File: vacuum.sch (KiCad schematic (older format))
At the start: 67 parts, among them J1 к БП, J10 геркон шибера 1, J11 запасной, J12 запасной, J13 к БП, J2 нагрузка, J3 нагрузка, J4 геркон клапана 0, J5 нагрузка, J6 нагрузка, J7 к БП, J8 геркон клапана 1, J9 геркон шибера 0, Q1 IRF740, Q2 IRF740, Q3 IRF740, Q4 IRF740, SW1 Кнопка, SW2 Кнопка, SW3 Кнопка, SW4 Выключить автоматику, SW5 Кнопка, U1 PC817, U10 PC817, U2 PC817, U3 PC817, U4 PC817, U5 PC817, U6 PC817, U7 PC817, U8 PC817, U9 PC817

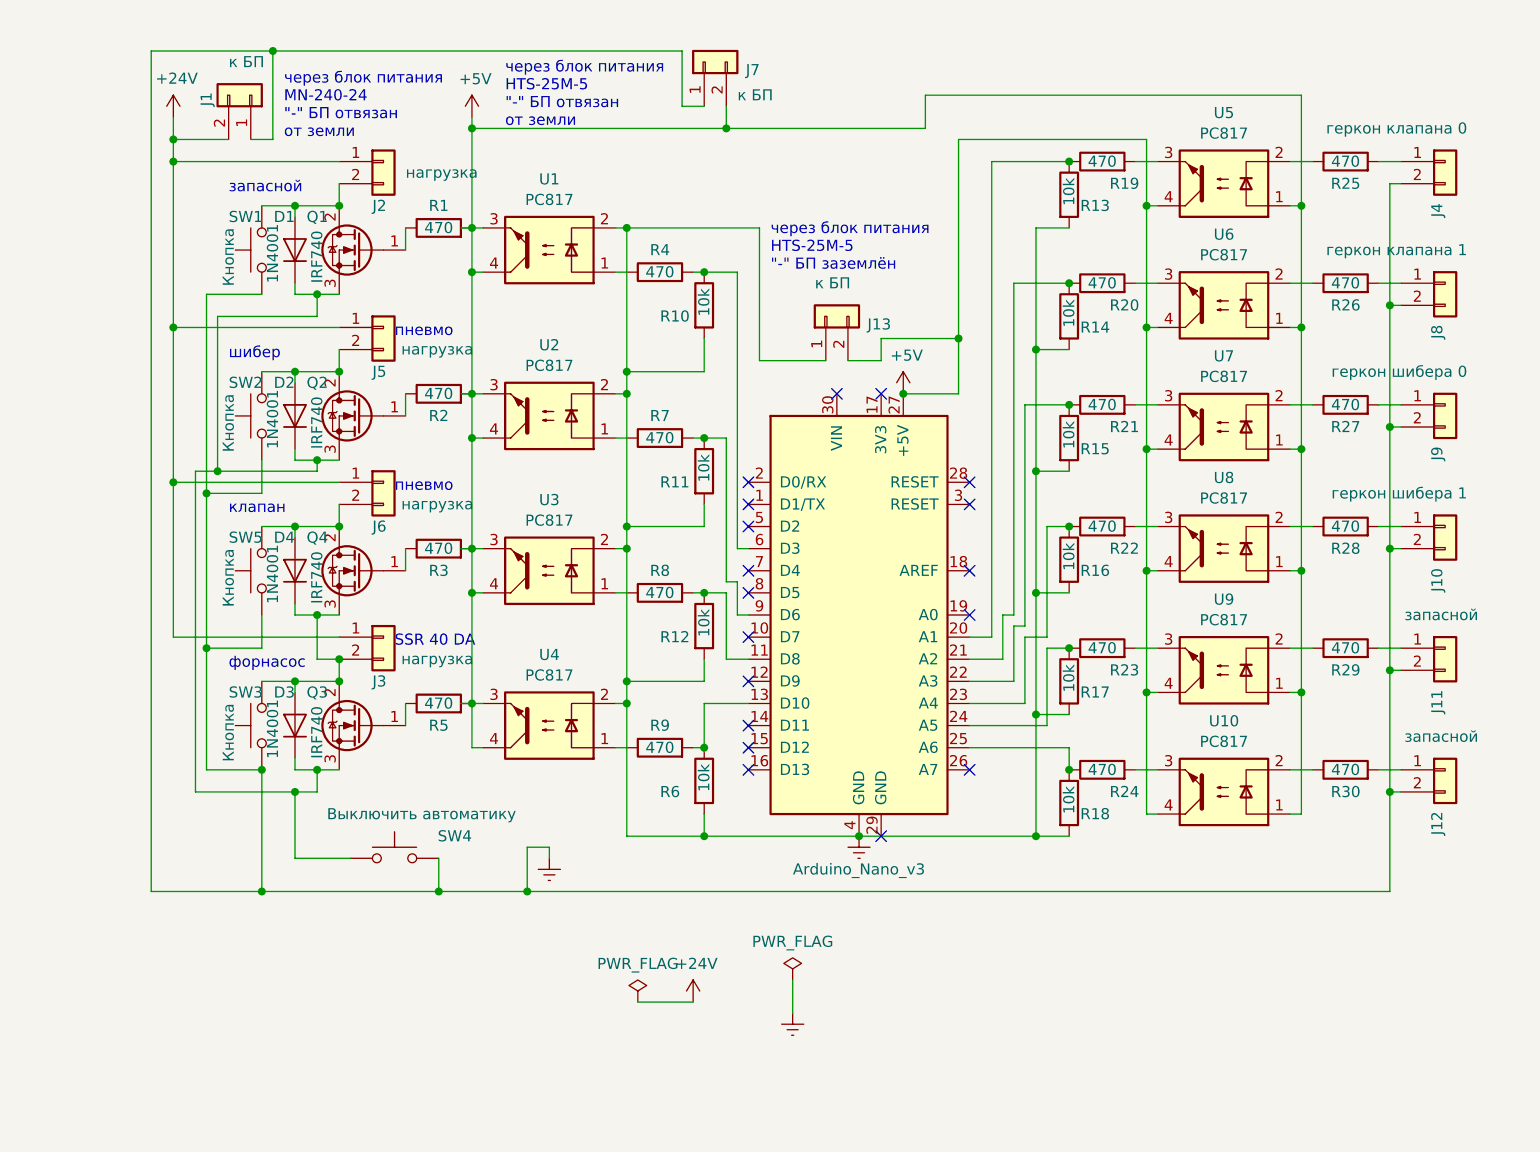
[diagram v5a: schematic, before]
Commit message: some important bags in *.sch removed, PCB partially created
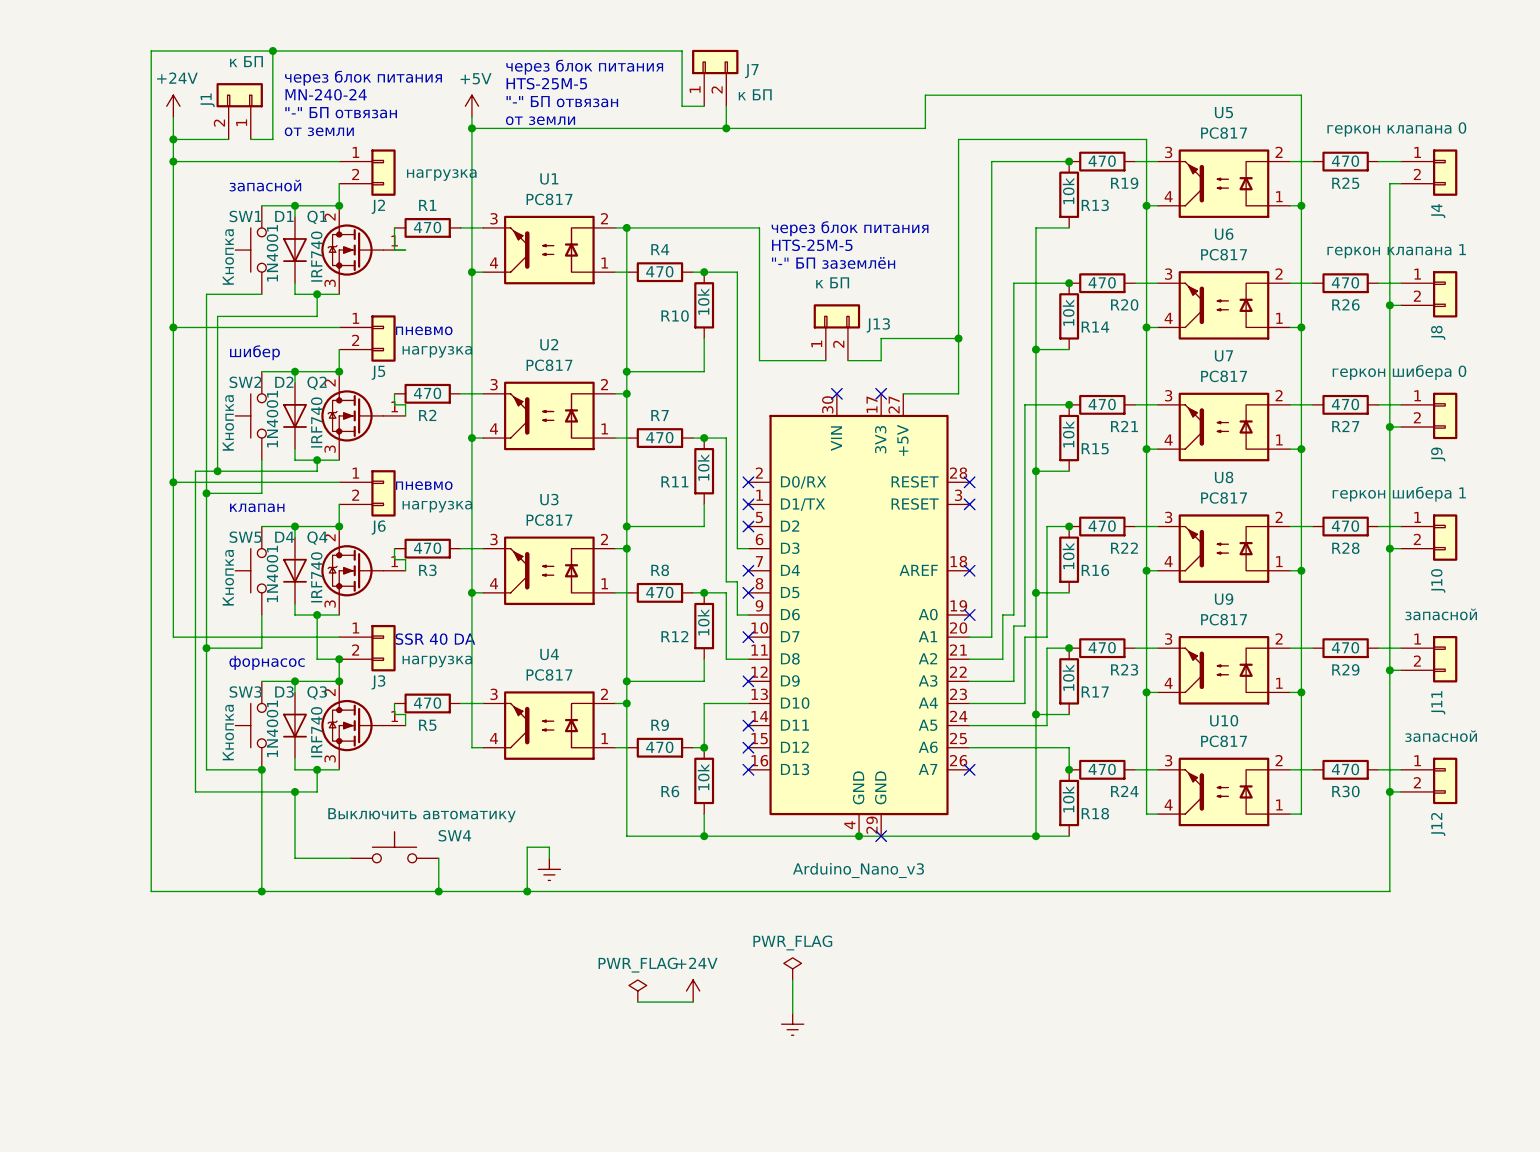
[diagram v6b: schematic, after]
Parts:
- SW1, SW2, SW3, SW5: footprint Button_Switch_THT:SW_PUSH_6mm_H5mm -> Connector_PinHeader_2.54mm:PinHeader_1x02_P2.54mm_Vertical
- SW4: footprint Button_Switch_THT:SW_PUSH_6mm -> TerminalBlock_Altech:Altech_AK300_1x02_P5.00mm_45-Degree
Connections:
- net +5V: no longer A1.27 (+5V), J13.2 (Pin_2), R1.2, R2.2, R3.2, R5.2, U1.3, U10.4, U2.3, U3.3, U4.3, U5.4, U6.4, U7.4, U8.4, U9.4
- net Earth: no longer A1.4 (GND), J13.1 (Pin_1), R10.2, R11.2, R12.2, R13.2, R14.2, R15.2, R16.2, R17.2, R18.2, R6.2, U1.2, U2.2, U3.2, U4.2
- new net: A1.27 (+5V), J13.2 (Pin_2), U10.4, U5.4, U6.4, U7.4, U8.4, U9.4
- new net: A1.4 (GND), J13.1 (Pin_1), R10.2, R11.2, R12.2, R13.2, R14.2, R15.2, R16.2, R17.2, R18.2, R6.2, U1.2, U2.2, U3.2, U4.2
- new net: R5.2, U4.3
- new net: R3.2, U3.3
- new net: R2.2, U2.3
- new net: R1.2, U1.3
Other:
- moved on the sheet: R1, R2, R3, R5

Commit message: vertical resistors aded
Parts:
- R1, R19, R2, R20, R21, R22, R23, R24, R25, R26, R27, R28, R29, R3, R30, R4, R7, R8, R9: footprint Resistor_THT:R_Axial_DIN0207_L6.3mm_D2.5mm_P7.62mm_Horizontal -> Resistor_THT:R_Axial_DIN0207_L6.3mm_D2.5mm_P5.08mm_Vertical
- R10, R11, R12, R13, R14, R15, R16, R17, R18, R6: footprint Resistor_THT:R_Axial_DIN0309_L9.0mm_D3.2mm_P12.70mm_Horizontal -> Resistor_THT:R_Axial_DIN0309_L9.0mm_D3.2mm_P5.08mm_Vertical
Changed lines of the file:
@@
 F 0 "R6" H 4050 5800 50  0000 L CNN
 F 1 "10k" V 4250 5800 50  0000 L CNN
-F 2 "Resistor_THT:R_Axial_DIN0309_L9.0mm_D3.2mm_P12.70mm_Horizontal" V 4180 5850 50  0001 C CNN
+F 2 "Resistor_THT:R_Axial_DIN0309_L9.0mm_D3.2mm_P5.08mm_Vertical" V 4180 5850 50  0001 C CNN
 F 3 "~" H 4250 5850 50  0001 C CNN
 	1    4250 5850
@@
 F 0 "R9" V 4150 5700 50  0000 C CNN
 F 1 "470" V 4050 5700 50  0000 C CNN
-F 2 "Resistor_THT:R_Axial_DIN0207_L6.3mm_D2.5mm_P7.62mm_Horizontal" V 3980 5700 50  0001 C CNN
+F 2 "Resistor_THT:R_Axial_DIN0207_L6.3mm_D2.5mm_P5.08mm_Vertical" V 3980 5700 50  0001 C CNN
 F 3 "~" H 4050 5700 50  0001 C CNN
 	1    4050 5700
@@
 F 0 "R12" H 4050 5100 50  0000 L CNN
 F 1 "10k" V 4250 5100 50  0000 L CNN
-F 2 "Resistor_THT:R_Axial_DIN0309_L9.0mm_D3.2mm_P12.70mm_Horizontal" V 4180 5150 50  0001 C CNN
+F 2 "Resistor_THT:R_Axial_DIN0309_L9.0mm_D3.2mm_P5.08mm_Vertical" V 4180 5150 50  0001 C CNN
 F 3 "~" H 4250 5150 50  0001 C CNN
 	1    4250 5150
@@
 F 0 "R8" V 4150 5000 50  0000 C CNN
 F 1 "470" V 4050 5000 50  0000 C CNN
-F 2 "Resistor_THT:R_Axial_DIN0207_L6.3mm_D2.5mm_P7.62mm_Horizontal" V 3980 5000 50  0001 C CNN
+F 2 "Resistor_THT:R_Axial_DIN0207_L6.3mm_D2.5mm_P5.08mm_Vertical" V 3980 5000 50  0001 C CNN
 F 3 "~" H 4050 5000 50  0001 C CNN
 	1    4050 5000
@@
 F 0 "R11" H 4050 4400 50  0000 L CNN
 F 1 "10k" V 4250 4400 50  0000 L CNN
-F 2 "Resistor_THT:R_Axial_DIN0309_L9.0mm_D3.2mm_P12.70mm_Horizontal" V 4180 4450 50  0001 C CNN
+F 2 "Resistor_THT:R_Axial_DIN0309_L9.0mm_D3.2mm_P5.08mm_Vertical" V 4180 4450 50  0001 C CNN
 F 3 "~" H 4250 4450 50  0001 C CNN
 	1    4250 4450
@@
 F 0 "R7" V 4150 4300 50  0000 C CNN
 F 1 "470" V 4050 4300 50  0000 C CNN
-F 2 "Resistor_THT:R_Axial_DIN0207_L6.3mm_D2.5mm_P7.62mm_Horizontal" V 3980 4300 50  0001 C CNN
+F 2 "Resistor_THT:R_Axial_DIN0207_L6.3mm_D2.5mm_P5.08mm_Vertical" V 3980 4300 50  0001 C CNN
 F 3 "~" H 4050 4300 50  0001 C CNN
 	1    4050 4300
@@
 F 0 "R1" V 3100 3350 50  0000 C CNN
 F 1 "470" V 3000 3350 50  0000 C CNN
-F 2 "Resistor_THT:R_Axial_DIN0207_L6.3mm_D2.5mm_P7.62mm_Horizontal" V 2930 3350 50  0001 C CNN
+F 2 "Resistor_THT:R_Axial_DIN0207_L6.3mm_D2.5mm_P5.08mm_Vertical" V 2930 3350 50  0001 C CNN
 F 3 "~" H 3000 3350 50  0001 C CNN
 	1    3000 3350
@@
 F 0 "R10" H 4050 3650 50  0000 L CNN
 F 1 "10k" V 4250 3650 50  0000 L CNN
-F 2 "Resistor_THT:R_Axial_DIN0309_L9.0mm_D3.2mm_P12.70mm_Horizontal" V 4180 3700 50  0001 C CNN
+F 2 "Resistor_THT:R_Axial_DIN0309_L9.0mm_D3.2mm_P5.08mm_Vertical" V 4180 3700 50  0001 C CNN
 F 3 "~" H 4250 3700 50  0001 C CNN
 	1    4250 3700
@@
 F 0 "R4" V 4150 3550 50  0000 C CNN
 F 1 "470" V 4050 3550 50  0000 C CNN
-F 2 "Resistor_THT:R_Axial_DIN0207_L6.3mm_D2.5mm_P7.62mm_Horizontal" V 3980 3550 50  0001 C CNN
+F 2 "Resistor_THT:R_Axial_DIN0207_L6.3mm_D2.5mm_P5.08mm_Vertical" V 3980 3550 50  0001 C CNN
 F 3 "~" H 4050 3550 50  0001 C CNN
 	1    4050 3550
@@
 F 0 "R24" V 5950 5700 50  0000 C CNN
 F 1 "470" V 6050 5800 50  0000 C CNN
-F 2 "Resistor_THT:R_Axial_DIN0207_L6.3mm_D2.5mm_P7.62mm_Horizontal" V 5980 5800 50  0001 C CNN
+F 2 "Resistor_THT:R_Axial_DIN0207_L6.3mm_D2.5mm_P5.08mm_Vertical" V 5980 5800 50  0001 C CNN
 F 3 "~" H 6050 5800 50  0001 C CNN
 	1    6050 5800
@@
 F 0 "R18" H 5950 5900 50  0000 L CNN
 F 1 "10k" V 5900 5900 50  0000 L CNN
-F 2 "Resistor_THT:R_Axial_DIN0309_L9.0mm_D3.2mm_P12.70mm_Horizontal" V 5830 5950 50  0001 C CNN
+F 2 "Resistor_THT:R_Axial_DIN0309_L9.0mm_D3.2mm_P5.08mm_Vertical" V 5830 5950 50  0001 C CNN
 F 3 "~" H 5900 5950 50  0001 C CNN
 	1    5900 5950
@@
 F 0 "R23" V 5950 5150 50  0000 C CNN
 F 1 "470" V 6050 5250 50  0000 C CNN
-F 2 "Resistor_THT:R_Axial_DIN0207_L6.3mm_D2.5mm_P7.62mm_Horizontal" V 5980 5250 50  0001 C CNN
+F 2 "Resistor_THT:R_Axial_DIN0207_L6.3mm_D2.5mm_P5.08mm_Vertical" V 5980 5250 50  0001 C CNN
 F 3 "~" H 6050 5250 50  0001 C CNN
 	1    6050 5250
@@
 F 0 "R17" H 5950 5350 50  0000 L CNN
 F 1 "10k" V 5900 5350 50  0000 L CNN
-F 2 "Resistor_THT:R_Axial_DIN0309_L9.0mm_D3.2mm_P12.70mm_Horizontal" V 5830 5400 50  0001 C CNN
+F 2 "Resistor_THT:R_Axial_DIN0309_L9.0mm_D3.2mm_P5.08mm_Vertical" V 5830 5400 50  0001 C CNN
 F 3 "~" H 5900 5400 50  0001 C CNN
 	1    5900 5400
@@
 F 0 "R22" V 5950 4600 50  0000 C CNN
 F 1 "470" V 6050 4700 50  0000 C CNN
-F 2 "Resistor_THT:R_Axial_DIN0207_L6.3mm_D2.5mm_P7.62mm_Horizontal" V 5980 4700 50  0001 C CNN
+F 2 "Resistor_THT:R_Axial_DIN0207_L6.3mm_D2.5mm_P5.08mm_Vertical" V 5980 4700 50  0001 C CNN
 F 3 "~" H 6050 4700 50  0001 C CNN
 	1    6050 4700
@@
 F 0 "R16" H 5950 4800 50  0000 L CNN
 F 1 "10k" V 5900 4800 50  0000 L CNN
-F 2 "Resistor_THT:R_Axial_DIN0309_L9.0mm_D3.2mm_P12.70mm_Horizontal" V 5830 4850 50  0001 C CNN
+F 2 "Resistor_THT:R_Axial_DIN0309_L9.0mm_D3.2mm_P5.08mm_Vertical" V 5830 4850 50  0001 C CNN
 F 3 "~" H 5900 4850 50  0001 C CNN
 	1    5900 4850
@@
 F 0 "R21" V 5950 4050 50  0000 C CNN
 F 1 "470" V 6050 4150 50  0000 C CNN
-F 2 "Resistor_THT:R_Axial_DIN0207_L6.3mm_D2.5mm_P7.62mm_Horizontal" V 5980 4150 50  0001 C CNN
+F 2 "Resistor_THT:R_Axial_DIN0207_L6.3mm_D2.5mm_P5.08mm_Vertical" V 5980 4150 50  0001 C CNN
 F 3 "~" H 6050 4150 50  0001 C CNN
 	1    6050 4150
@@
 F 0 "R15" H 5950 4250 50  0000 L CNN
 F 1 "10k" V 5900 4250 50  0000 L CNN
-F 2 "Resistor_THT:R_Axial_DIN0309_L9.0mm_D3.2mm_P12.70mm_Horizontal" V 5830 4300 50  0001 C CNN
+F 2 "Resistor_THT:R_Axial_DIN0309_L9.0mm_D3.2mm_P5.08mm_Vertical" V 5830 4300 50  0001 C CNN
 F 3 "~" H 5900 4300 50  0001 C CNN
 	1    5900 4300
@@
 F 0 "R20" V 5950 3500 50  0000 C CNN
 F 1 "470" V 6050 3600 50  0000 C CNN
-F 2 "Resistor_THT:R_Axial_DIN0207_L6.3mm_D2.5mm_P7.62mm_Horizontal" V 5980 3600 50  0001 C CNN
+F 2 "Resistor_THT:R_Axial_DIN0207_L6.3mm_D2.5mm_P5.08mm_Vertical" V 5980 3600 50  0001 C CNN
 F 3 "~" H 6050 3600 50  0001 C CNN
 	1    6050 3600
@@
 F 0 "R14" H 5950 3700 50  0000 L CNN
 F 1 "10k" V 5900 3700 50  0000 L CNN
-F 2 "Resistor_THT:R_Axial_DIN0309_L9.0mm_D3.2mm_P12.70mm_Horizontal" V 5830 3750 50  0001 C CNN
+F 2 "Resistor_THT:R_Axial_DIN0309_L9.0mm_D3.2mm_P5.08mm_Vertical" V 5830 3750 50  0001 C CNN
 F 3 "~" H 5900 3750 50  0001 C CNN
 	1    5900 3750
@@
 F 0 "R19" V 5950 2950 50  0000 C CNN
 F 1 "470" V 6050 3050 50  0000 C CNN
-F 2 "Resistor_THT:R_Axial_DIN0207_L6.3mm_D2.5mm_P7.62mm_Horizontal" V 5980 3050 50  0001 C CNN
+F 2 "Resistor_THT:R_Axial_DIN0207_L6.3mm_D2.5mm_P5.08mm_Vertical" V 5980 3050 50  0001 C CNN
 F 3 "~" H 6050 3050 50  0001 C CNN
 	1    6050 3050
@@
 F 0 "R13" H 5950 3150 50  0000 L CNN
 F 1 "10k" V 5900 3150 50  0000 L CNN
-F 2 "Resistor_THT:R_Axial_DIN0309_L9.0mm_D3.2mm_P12.70mm_Horizontal" V 5830 3200 50  0001 C CNN
+F 2 "Resistor_THT:R_Axial_DIN0309_L9.0mm_D3.2mm_P5.08mm_Vertical" V 5830 3200 50  0001 C CNN
 F 3 "~" H 5900 3200 50  0001 C CNN
 	1    5900 3200
@@
 F 0 "R25" V 7050 3050 50  0000 C CNN
 F 1 "470" V 7150 3050 50  0000 C CNN
-F 2 "Resistor_THT:R_Axial_DIN0207_L6.3mm_D2.5mm_P7.62mm_Horizontal" V 7080 3050 50  0001 C CNN
+F 2 "Resistor_THT:R_Axial_DIN0207_L6.3mm_D2.5mm_P5.08mm_Vertical" V 7080 3050 50  0001 C CNN
 F 3 "~" H 7150 3050 50  0001 C CNN
 	1    7150 3050
@@
 F 0 "R26" V 7050 3600 50  0000 C CNN
 F 1 "470" V 7150 3600 50  0000 C CNN
-F 2 "Resistor_THT:R_Axial_DIN0207_L6.3mm_D2.5mm_P7.62mm_Horizontal" V 7080 3600 50  0001 C CNN
+F 2 "Resistor_THT:R_Axial_DIN0207_L6.3mm_D2.5mm_P5.08mm_Vertical" V 7080 3600 50  0001 C CNN
 F 3 "~" H 7150 3600 50  0001 C CNN
 	1    7150 3600
@@
 F 0 "R27" V 7050 4150 50  0000 C CNN
 F 1 "470" V 7150 4150 50  0000 C CNN
-F 2 "Resistor_THT:R_Axial_DIN0207_L6.3mm_D2.5mm_P7.62mm_Horizontal" V 7080 4150 50  0001 C CNN
+F 2 "Resistor_THT:R_Axial_DIN0207_L6.3mm_D2.5mm_P5.08mm_Vertical" V 7080 4150 50  0001 C CNN
 F 3 "~" H 7150 4150 50  0001 C CNN
 	1    7150 4150
@@
 F 0 "R28" V 7050 4700 50  0000 C CNN
 F 1 "470" V 7150 4700 50  0000 C CNN
-F 2 "Resistor_THT:R_Axial_DIN0207_L6.3mm_D2.5mm_P7.62mm_Horizontal" V 7080 4700 50  0001 C CNN
+F 2 "Resistor_THT:R_Axial_DIN0207_L6.3mm_D2.5mm_P5.08mm_Vertical" V 7080 4700 50  0001 C CNN
 F 3 "~" H 7150 4700 50  0001 C CNN
 	1    7150 4700
@@
 F 0 "R29" V 7050 5250 50  0000 C CNN
 F 1 "470" V 7150 5250 50  0000 C CNN
-F 2 "Resistor_THT:R_Axial_DIN0207_L6.3mm_D2.5mm_P7.62mm_Horizontal" V 7080 5250 50  0001 C CNN
+F 2 "Resistor_THT:R_Axial_DIN0207_L6.3mm_D2.5mm_P5.08mm_Vertical" V 7080 5250 50  0001 C CNN
 F 3 "~" H 7150 5250 50  0001 C CNN
 	1    7150 5250
@@
 F 0 "R30" V 7050 5800 50  0000 C CNN
 F 1 "470" V 7150 5800 50  0000 C CNN
-F 2 "Resistor_THT:R_Axial_DIN0207_L6.3mm_D2.5mm_P7.62mm_Horizontal" V 7080 5800 50  0001 C CNN
+F 2 "Resistor_THT:R_Axial_DIN0207_L6.3mm_D2.5mm_P5.08mm_Vertical" V 7080 5800 50  0001 C CNN
 F 3 "~" H 7150 5800 50  0001 C CNN
 	1    7150 5800
@@
 F 0 "R3" V 2900 4800 50  0000 C CNN
 F 1 "470" V 3000 4800 50  0000 C CNN
-F 2 "Resistor_THT:R_Axial_DIN0207_L6.3mm_D2.5mm_P7.62mm_Horizontal" V 2930 4800 50  0001 C CNN
+F 2 "Resistor_THT:R_Axial_DIN0207_L6.3mm_D2.5mm_P5.08mm_Vertical" V 2930 4800 50  0001 C CNN
 F 3 "~" H 3000 4800 50  0001 C CNN
 	1    3000 4800
@@
 F 0 "R2" V 2900 4100 50  0000 C CNN
 F 1 "470" V 3000 4100 50  0000 C CNN
-F 2 "Resistor_THT:R_Axial_DIN0207_L6.3mm_D2.5mm_P7.62mm_Horizontal" V 2930 4100 50  0001 C CNN
+F 2 "Resistor_THT:R_Axial_DIN0207_L6.3mm_D2.5mm_P5.08mm_Vertical" V 2930 4100 50  0001 C CNN
 F 3 "~" H 3000 4100 50  0001 C CNN
 	1    3000 4100
